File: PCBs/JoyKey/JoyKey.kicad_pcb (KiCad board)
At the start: 2 copper layers, 100 x 56.8 mm, 52 parts, among them J1 OLED_DISPLAY, J2 Conn_01x03_Socket, J3 Testpad wire hole1, J4 JST PH, J5 Top Trigger 1, J6 Top Trigger 2, Q1 PMOS,Si7157DP, SW1 RotaryEncoder_Switch, SW2 SW_Push_45deg, SW3 SW_Push_45deg, SW4 SW_Push_45deg, SW5 SW_Push_45deg, SW6 SW_Push_45deg, SW7 SW_Push_45deg, U1 BQ25060, U3 XIAO-RP2040-DIP, U4 LP2981-3.3, U5 2_axis_analog_joystick_button

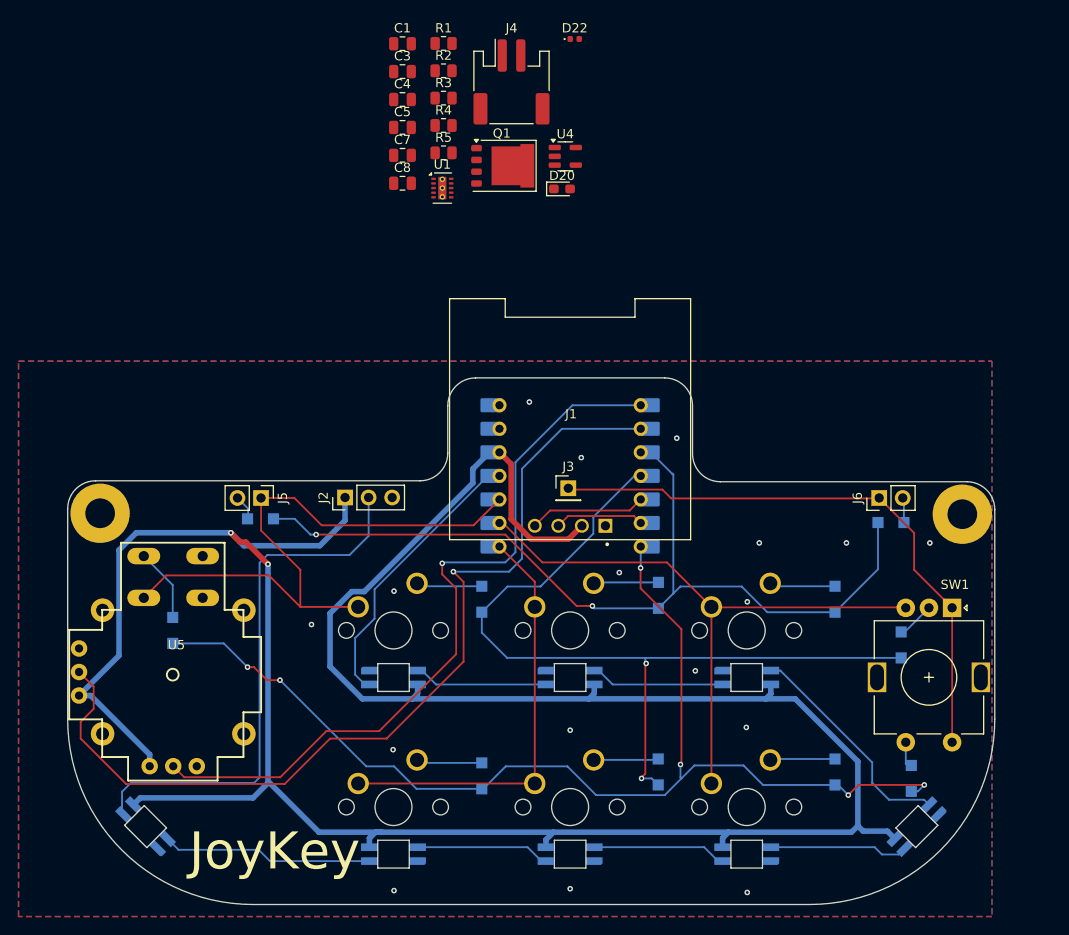
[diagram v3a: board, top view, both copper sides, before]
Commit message: Adjusted display to be in PCB center instead of keypad center
It looks better now, originally I wanted the whole display to be centered for the whole device, but I think I may end up using the verticle encoder and having the pcb be the final shape
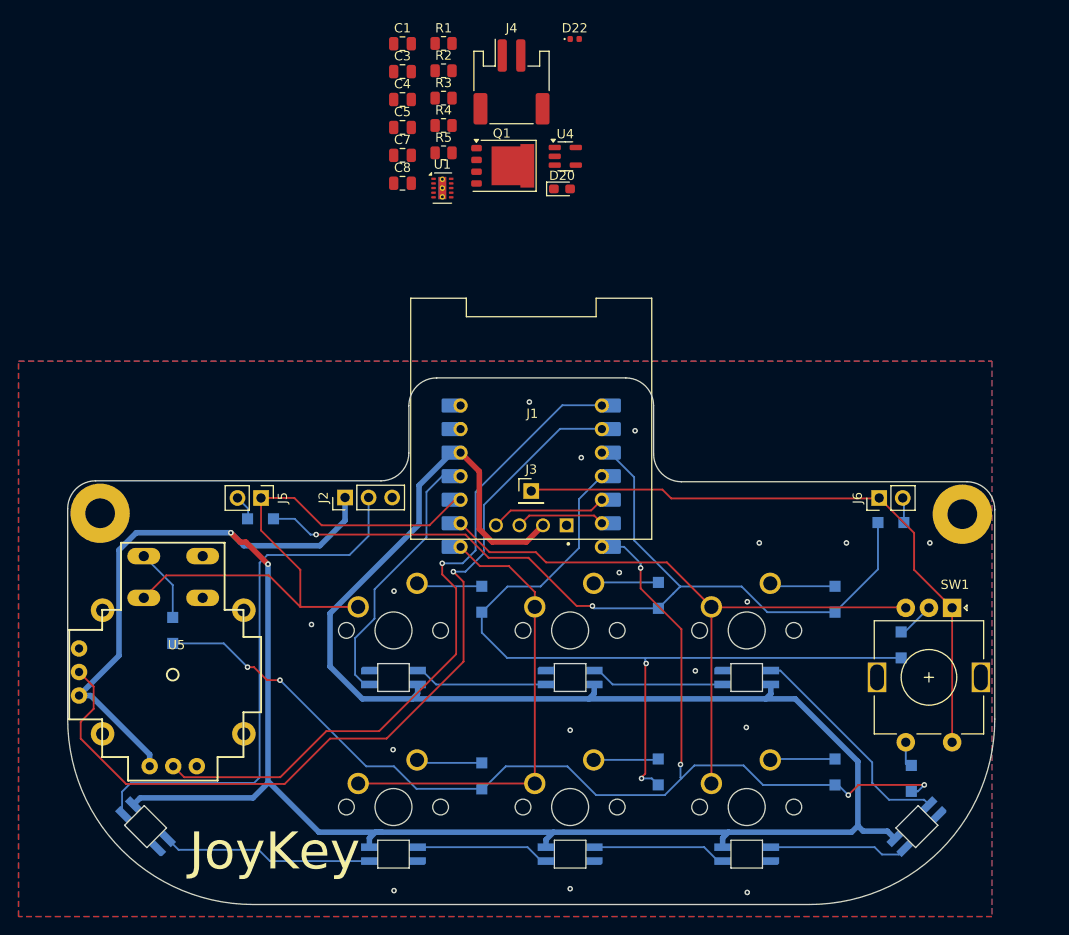
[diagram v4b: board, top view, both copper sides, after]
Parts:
- moved J1 4.19 mm to (136.3, 86.7)
- moved U3 4.19 mm to (136.3, 92.9)
- moved J3 4.01 mm to (136.3, 94.5)
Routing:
- net /JoystickY: track 99.6 -> 92.8 mm
- net /JoystickX: track 81.1 -> 75.1 mm
- net /COL2: track 66.7 -> 70.9 mm
- net /COL0: track 67.1 -> 62.9 mm
- net /COL3: track 63.6 -> 67.6 mm
- net /COL1: track 46.2 -> 49.7 mm
- net /ROW2: track 121.9 -> 125.0 mm
- net +3V3: track 302.0 -> 299.9 mm
- net /ROW1: track 88.2 -> 86.0 mm
- net /WS2812B: track 29.8 -> 28.5 mm
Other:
- outline, holes or cut-outs redrawn

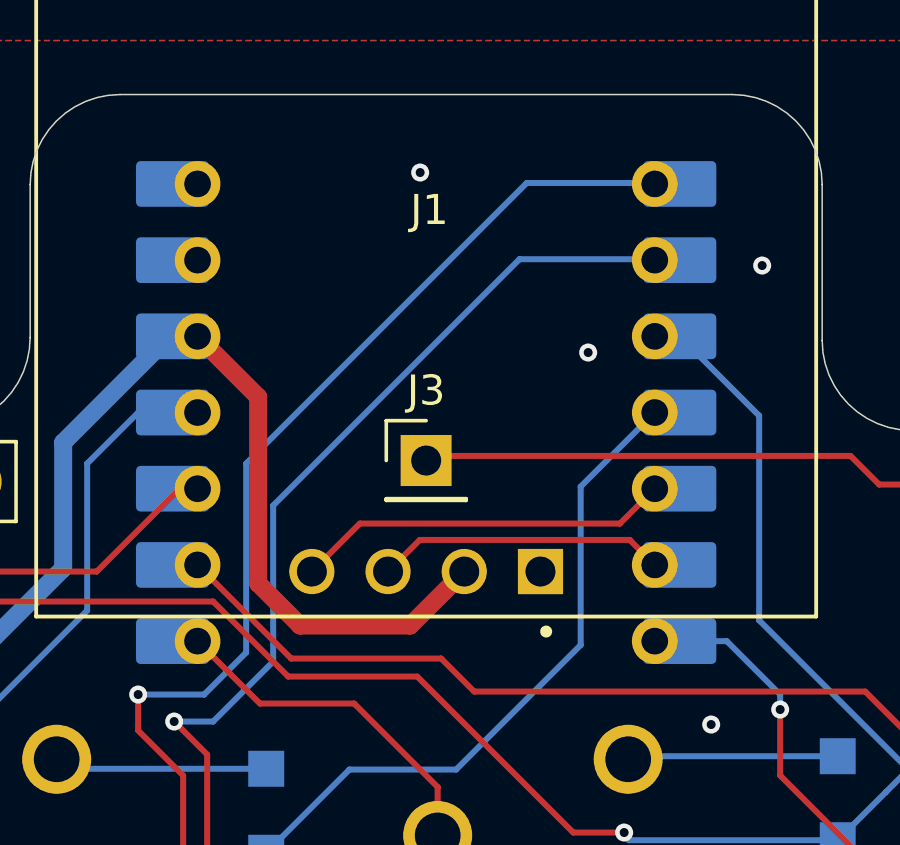
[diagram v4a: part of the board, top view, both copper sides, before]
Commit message: Added Accel and Gyro sensor
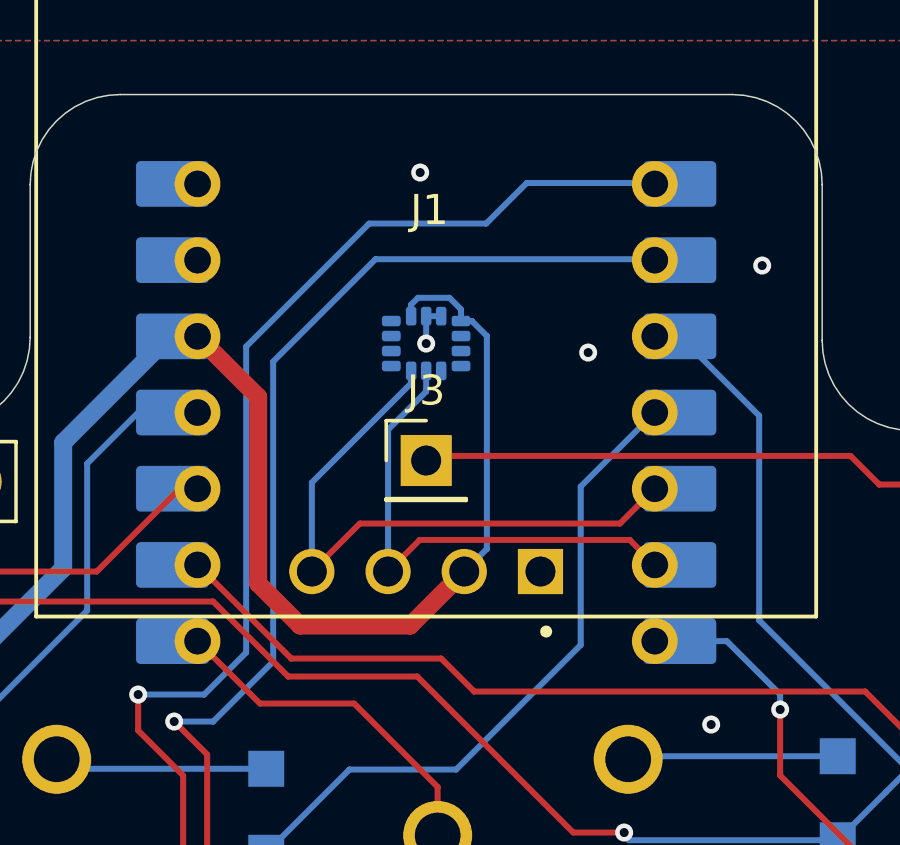
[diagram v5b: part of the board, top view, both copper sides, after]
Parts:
- added U2: LSM6DSL, Package_LGA:LGA-14_3x2.5mm_P0.5mm_LayoutBorder3x4y, B.Cu at (136.3, 90.6)
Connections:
- net SCL renamed /SCL
- net SDA renamed /SDA
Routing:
- net +3V3: track 299.9 -> 311.8 mm
- net /SDA: track 12.6 -> 20.6 mm
- net /SCL: track 9.67 -> 16.9 mm
- net /JoystickY: track 92.8 -> 95.6 mm
- net /JoystickX: track 75.1 -> 77.3 mm
- net GND: track 0.37 -> 1.78 mm, vias 17 -> 18

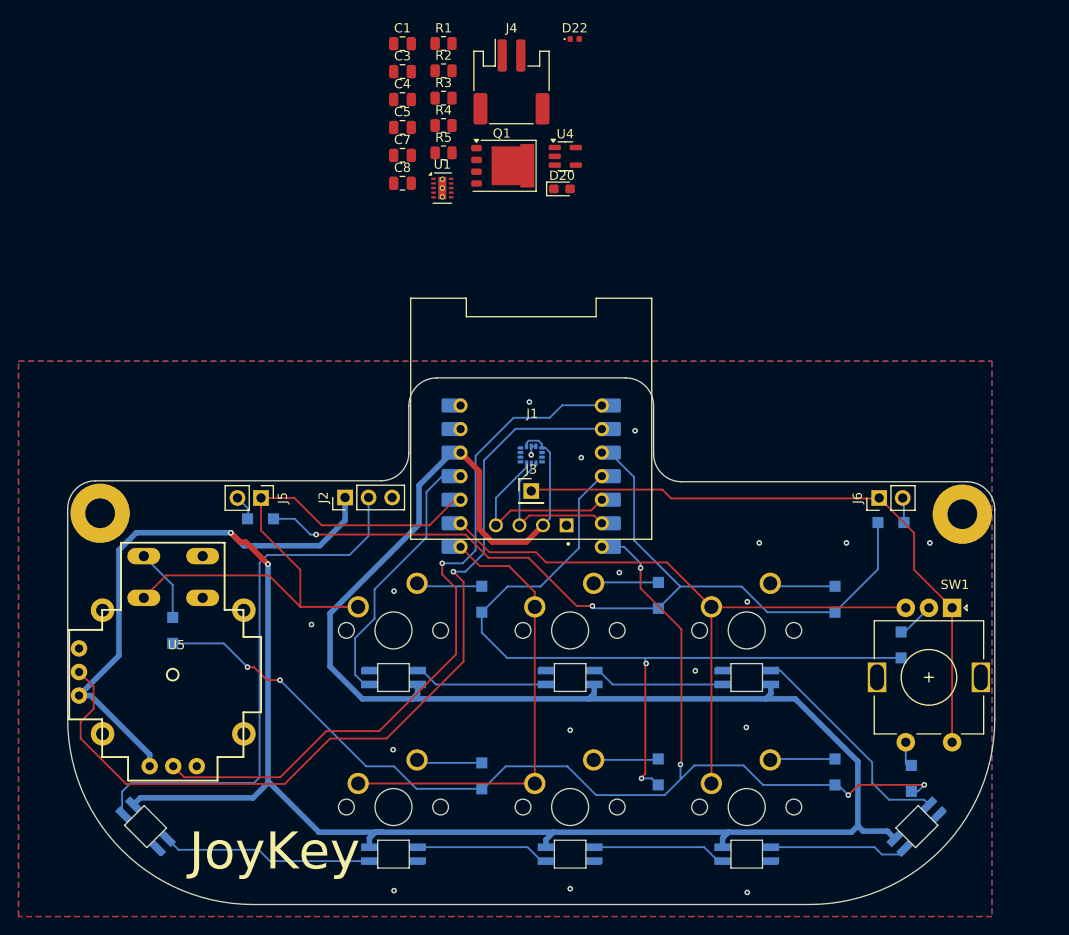
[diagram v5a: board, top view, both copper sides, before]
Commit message: Adjusted silkscreen text and added custom font
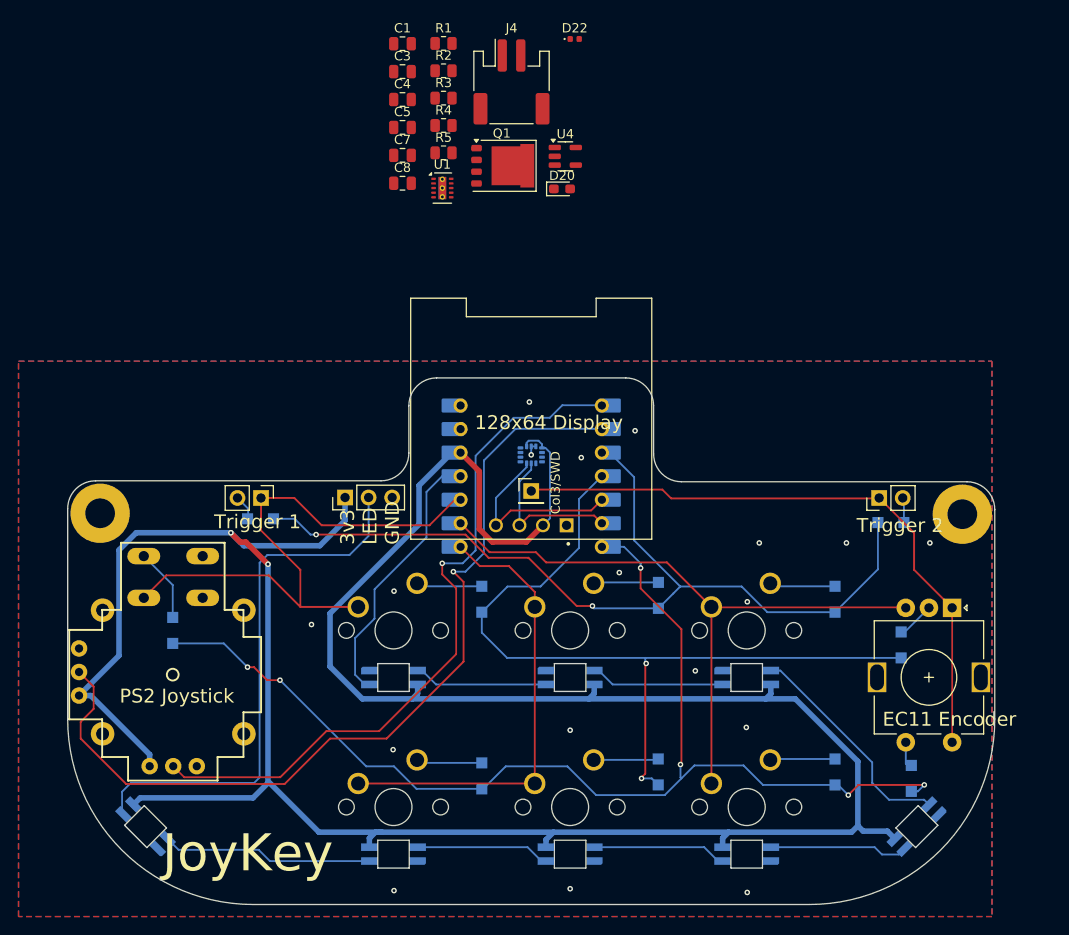
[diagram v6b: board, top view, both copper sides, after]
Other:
- board text added: "128x64 Display"
- board text added: "3v3 LED GND"
- board text added: "Col3/SWD"
- board text added: "EC11 Encoder"
- board text added: "PS2 Joystick"
- board text added: "Trigger 1"
- board text added: "Trigger 2"
- board text removed: "12mm"
- board text removed: "14mm"

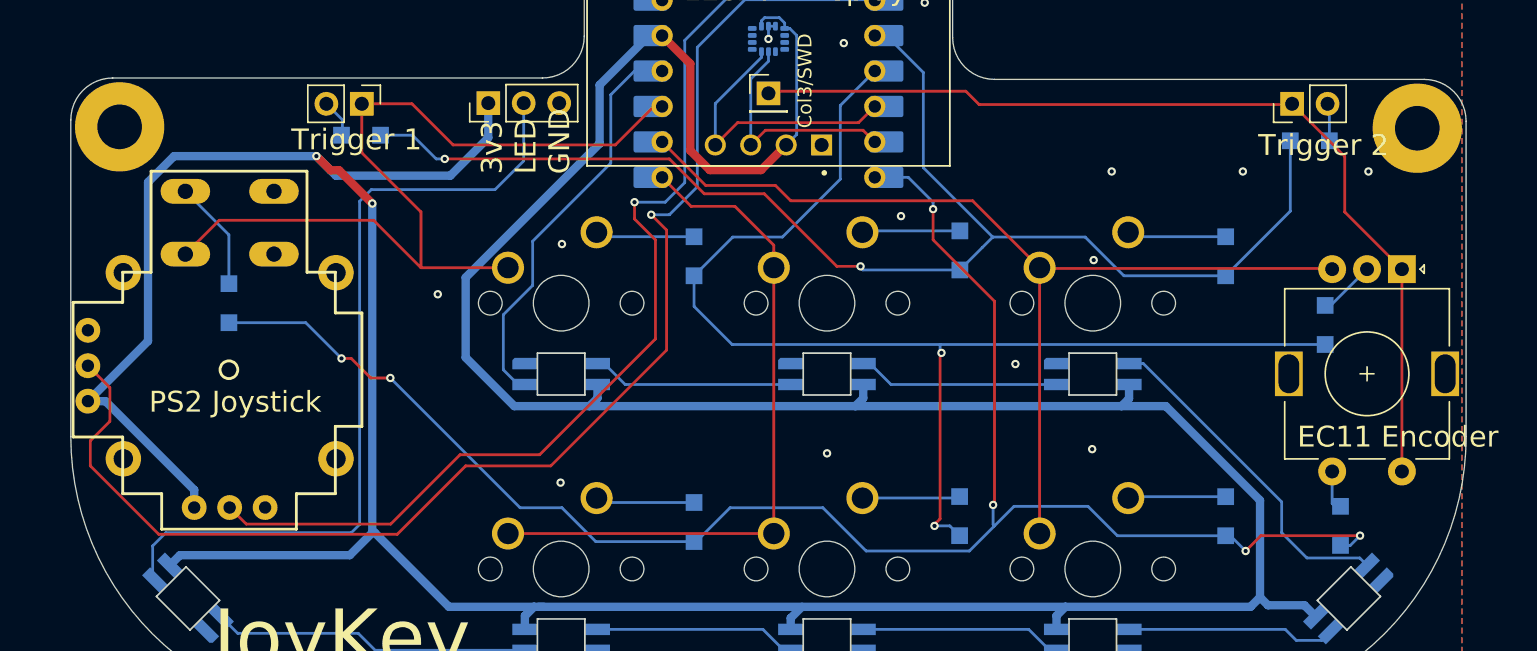
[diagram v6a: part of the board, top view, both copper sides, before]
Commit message: Added 2 extra LEDs
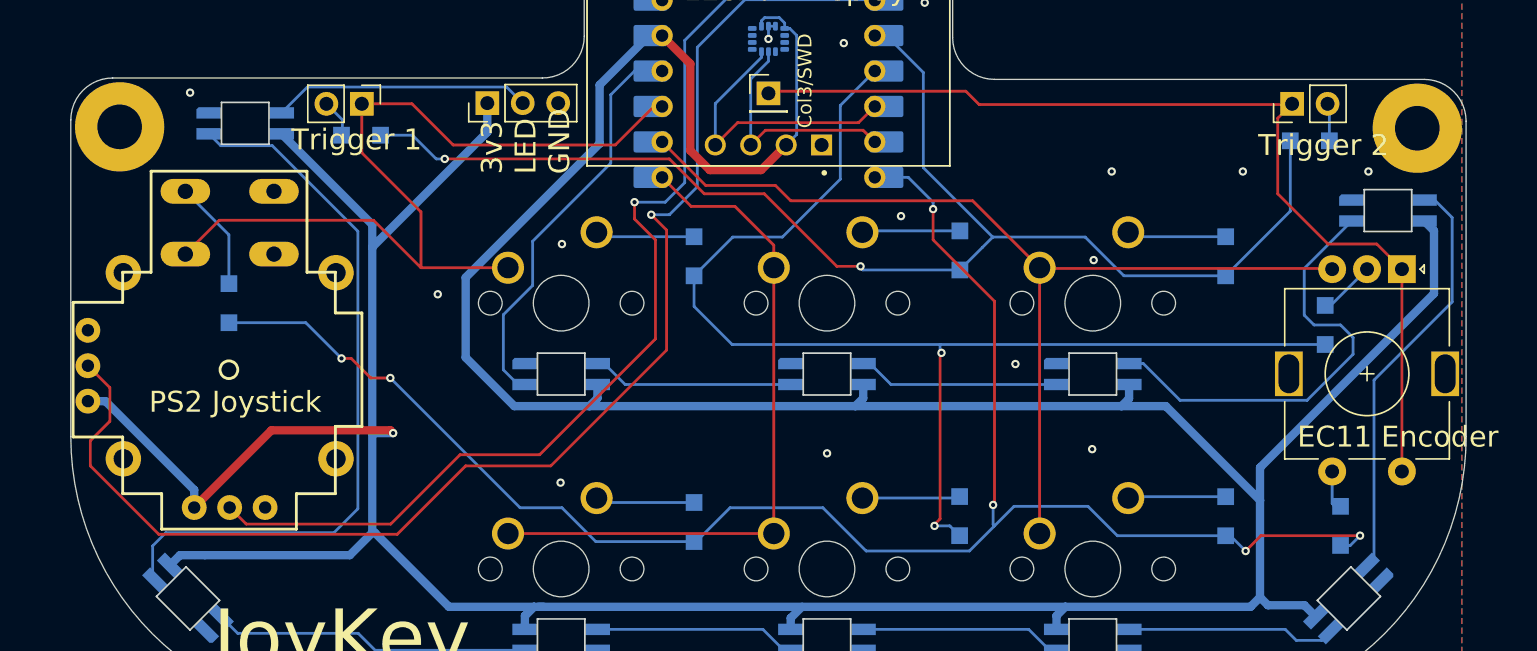
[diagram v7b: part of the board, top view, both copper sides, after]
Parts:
- added D13: SK6812MINI, SK6812MINI-E:SK6812MINI-E, B.Cu at (180.7, 102.9)
- added D23: SK6812MINI, SK6812MINI-E:SK6812MINI-E, B.Cu at (98.8, 96.7)
- moved J2 0.07 mm to (116.2, 95.2)
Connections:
- D6 pad 1: Net-(D6-DOUT) -> Net-(D13-DIN)
- D7 pad 3: Net-(D6-DOUT) -> Net-(D13-DOUT)
- J2 pad 2: Net-(D19-DOUT) -> Net-(D23-DOUT)
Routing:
- net Net-(D13-DIN): track 0.00 -> 32.0 mm
- net Net-(D13-DOUT): track 0.00 -> 30.0 mm
- net Net-(D6-DOUT): track 24.3 -> 0.00 mm
- net Net-(D23-DOUT): track 0.00 -> 18.5 mm
- net +3V3: track 311.8 -> 324.6 mm, vias 2 -> 1
- net Net-(D19-DOUT): track 58.3 -> 51.8 mm
- net /COL3: track 67.6 -> 70.5 mm
- net GND: vias 18 -> 19
